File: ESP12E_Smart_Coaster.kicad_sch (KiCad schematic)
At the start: 13 parts

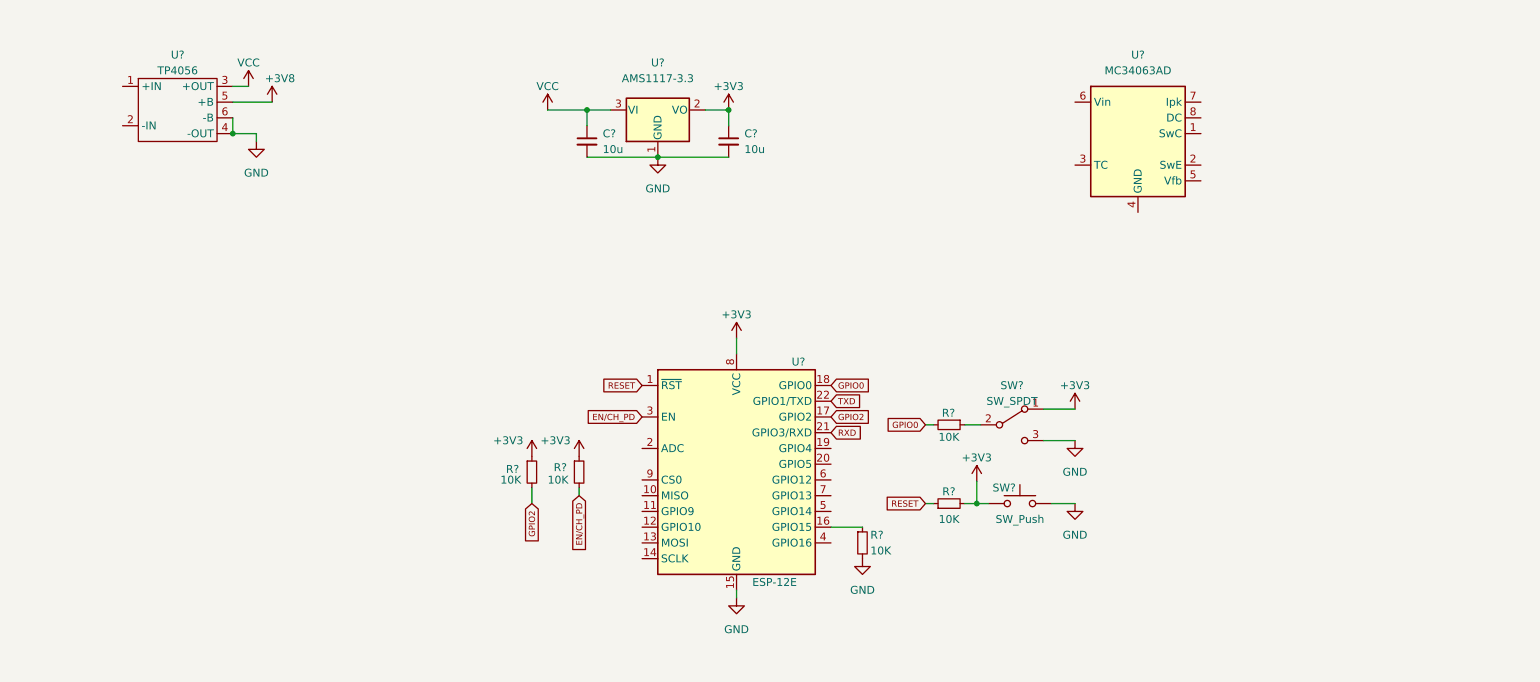
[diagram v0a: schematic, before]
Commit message: add voltage booster
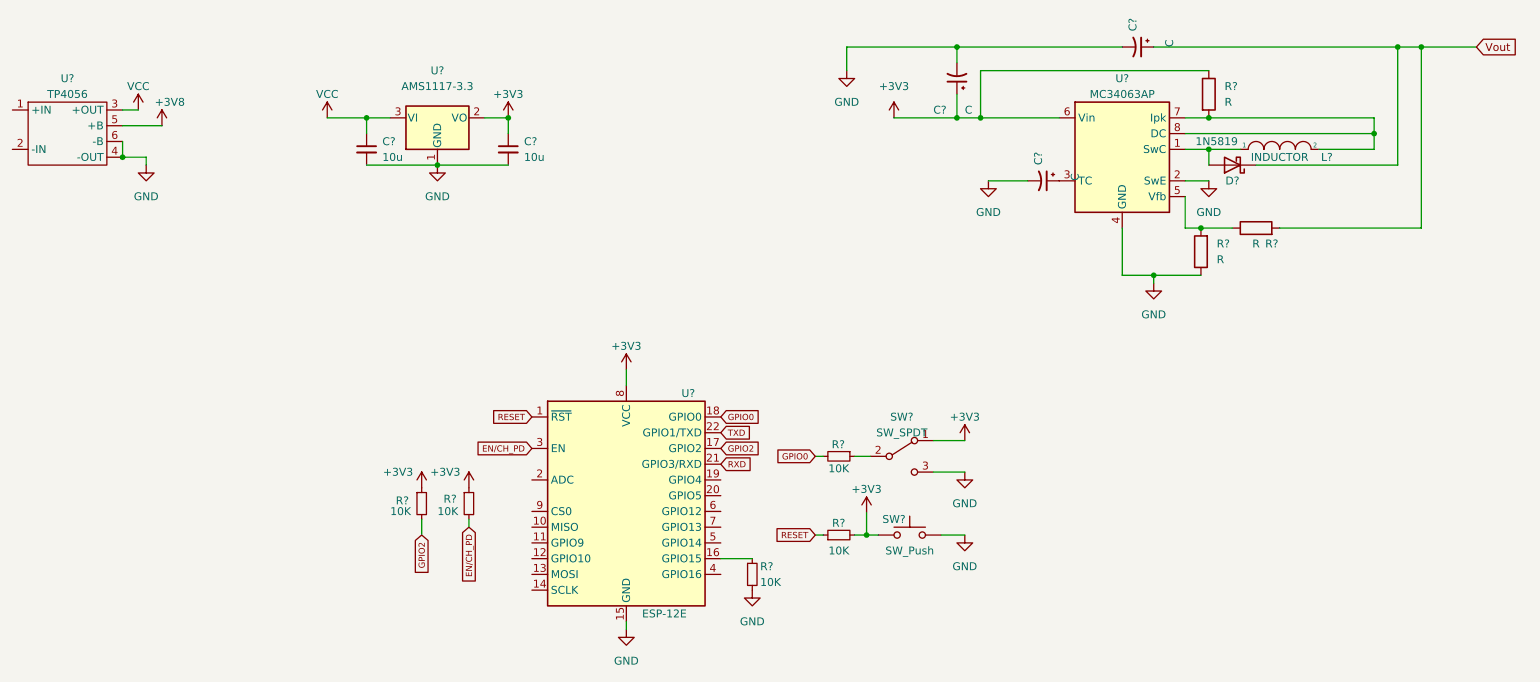
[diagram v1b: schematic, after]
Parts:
- removed U?: MC34063AD, Package_SO:SOIC-8_3.9x4.9mm_P1.27mm, symbol Regulator_Switching:MC34063AD
- added C? (x3): C, symbol Device:C_Polarized_Small_US
- added D?: 1N5819, Diode_THT:D_DO-41_SOD81_P10.16mm_Horizontal, symbol Diode:1N5819
- added L?: INDUCTOR, symbol pspice:INDUCTOR
- added R? (x3): R, symbol Device:R
- added U?: MC34063AP, Package_DIP:DIP-8_W7.62mm, symbol Regulator_Switching:MC34063AP
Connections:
- net +3V3: now also C?.1, R?.1, U?.6 (Vin)
- net GND: now also C?.2, C?.2, C?.2, R?.1, U?.2 (SwE), U?.4 (GND)
- new net: L?.2, R?.2, U?.7 (Ipk), U?.8 (DC)
- new net: D?.2 (A), L?.1, U?.1 (SwC)
- new net: C?.1, U?.3 (TC)
- new net: R?.1, R?.2, U?.5 (Vfb)
- new net Vout: C?.1, D?.1 (K), R?.2
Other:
- moved on the sheet: C?, R?, SW?, U?

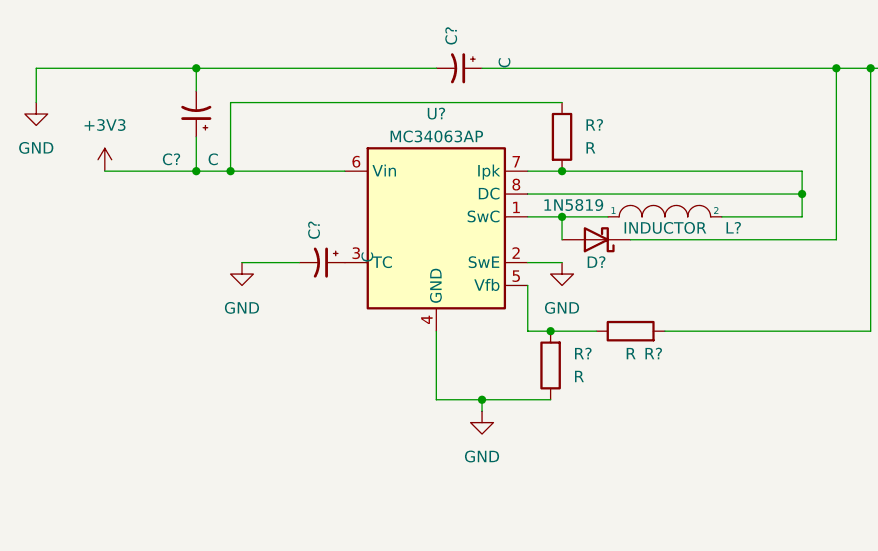
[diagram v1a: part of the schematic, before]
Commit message: add components value
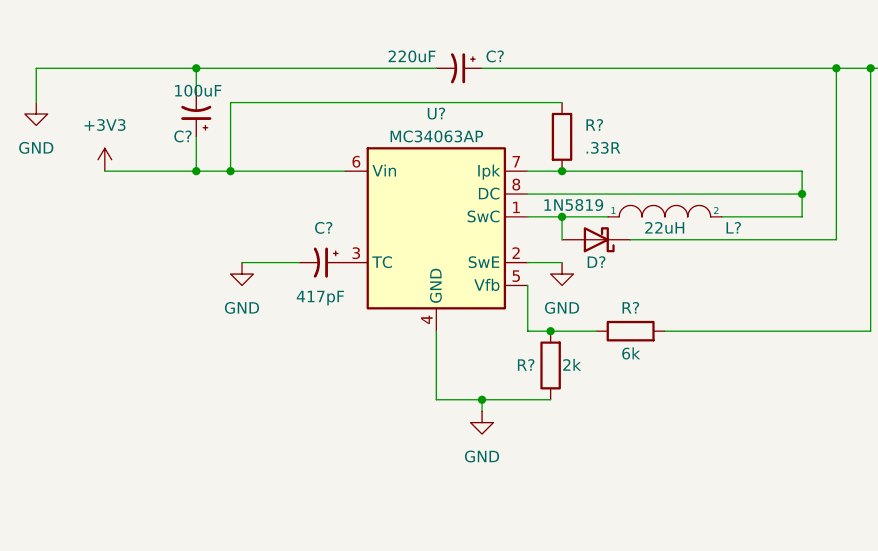
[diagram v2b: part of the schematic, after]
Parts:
- C?: value C -> 220uF
- C?: value C -> 417pF
- C?: value C -> 100uF
- L?: value INDUCTOR -> 22uH
- R?: value R -> .33R
- R?: value R -> 2k
- R?: value R -> 6k
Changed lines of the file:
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@@
   (symbol (lib_id "Device:C_Polarized_Small_US") (at 209.55 22.86 270) (unit 1)
     (in_bom yes) (on_board yes)
-    (property "Reference" "C?" (id 0) (at 208.7117 20.32 0)
+    (property "Reference" "C?" (id 0) (at 214.63 21.59 90)
       (effects (font (size 1.27 1.27)) (justify right))
     )
-    (property "Value" "C" (id 1) (at 214.63 22.86 0)
+    (property "Value" "220uF" (id 1) (at 207.01 21.59 90)
       (effects (font (size 1.27 1.27)) (justify right))
     )
@@
       (effects (font (size 1.27 1.27)) (justify left))
     )
-    (property "Value" "R" (id 1) (at 223.52 31.7499 0)
+    (property "Value" ".33R" (id 1) (at 223.52 31.7499 0)
       (effects (font (size 1.27 1.27)) (justify left))
     )
@@
   (symbol (lib_id "Device:C_Polarized_Small_US") (at 194.31 44.45 270) (unit 1)
     (in_bom yes) (on_board yes)
-    (property "Reference" "C?" (id 0) (at 193.4717 41.91 0)
+    (property "Reference" "C?" (id 0) (at 195.58 40.64 90)
       (effects (font (size 1.27 1.27)) (justify right))
     )
-    (property "Value" "C" (id 1) (at 199.39 44.45 0)
+    (property "Value" "417pF" (id 1) (at 196.85 48.26 90)
       (effects (font (size 1.27 1.27)) (justify right))
     )
@@
   )
   (symbol (lib_id "Device:R") (at 219.71 55.88 180) (unit 1)
-    (in_bom yes) (on_board yes) (fields_autoplaced)
-    (property "Reference" "R?" (id 0) (at 222.25 54.6099 0)
+    (in_bom yes) (on_board yes)
+    (property "Reference" "R?" (id 0) (at 215.9 55.88 0)
       (effects (font (size 1.27 1.27)) (justify right))
     )
-    (property "Value" "R" (id 1) (at 222.25 57.1499 0)
+    (property "Value" "2k" (id 1) (at 220.98 55.88 0)
       (effects (font (size 1.27 1.27)) (justify right))
     )
@@
   (symbol (lib_id "Device:R") (at 228.6 52.07 90) (unit 1)
     (in_bom yes) (on_board yes)
-    (property "Reference" "R?" (id 0) (at 231.14 54.61 90))
-    (property "Value" "R" (id 1) (at 228.6 54.61 90))
+    (property "Reference" "R?" (id 0) (at 228.6 49.53 90))
+    (property "Value" "6k" (id 1) (at 228.6 54.61 90))
     (property "Footprint" "" (id 2) (at 228.6 53.848 90)
       (effects (font (size 1.27 1.27)) hide)
@@
     (in_bom yes) (on_board yes)
     (property "Reference" "L?" (id 0) (at 240.03 40.64 0))
-    (property "Value" "INDUCTOR" (id 1) (at 232.41 40.64 0))
+    (property "Value" "22uH" (id 1) (at 232.41 40.64 0))
     (property "Footprint" "" (id 2) (at 232.41 39.37 0)
       (effects (font (size 1.27 1.27)) hide)
@@
   (symbol (lib_id "Device:C_Polarized_Small_US") (at 180.34 27.94 180) (unit 1)
     (in_bom yes) (on_board yes)
-    (property "Reference" "C?" (id 0) (at 176.53 33.02 0)
+    (property "Reference" "C?" (id 0) (at 177.8 30.48 0)
       (effects (font (size 1.27 1.27)) (justify right))
     )
-    (property "Value" "C" (id 1) (at 181.61 33.02 0)
+    (property "Value" "100uF" (id 1) (at 177.8 25.4 0)
       (effects (font (size 1.27 1.27)) (justify right))
     )
@@
     )
     (path "/03ffd44a-5907-4c69-ac63-01d05e10d185"
-      (reference "C?") (unit 1) (value "C") (footprint "")
+      (reference "C?") (unit 1) (value "220uF") (footprint "")
     )
     (path "/29977eb4-9adf-45f9-b113-8a6b672d0704"
@@
     )
     (path "/9a08c8ca-4c0a-4e75-ad14-947e63ea15d1"
-      (reference "C?") (unit 1) (value "C") (footprint "")
+      (reference "C?") (unit 1) (value "417pF") (footprint "")
     )
     (path "/ec0d531d-d013-4299-bad6-1fe86c606b21"
-      (reference "C?") (unit 1) (value "C") (footprint "")
+      (reference "C?") (unit 1) (value "100uF") (footprint "")
     )
     (path "/2ac1246d-9c49-4a5b-b077-d0142a22f5d7"
@@
     )
     (path "/e59b00a5-38a1-4381-bbb6-aa74cdba2304"
-      (reference "L?") (unit 1) (value "INDUCTOR") (footprint "")
+      (reference "L?") (unit 1) (value "22uH") (footprint "")
     )
     (path "/1b0e959e-9bed-4bef-ad44-07b27cb59bfc"
@@
     )
     (path "/1c0d1c3e-a71c-43a5-a634-2d8857ddc607"
-      (reference "R?") (unit 1) (value "R") (footprint "")
+      (reference "R?") (unit 1) (value ".33R") (footprint "")
     )
     (path "/28df4517-a8ac-43e7-b247-120822e55e22"
@@
     )
     (path "/a36cbb74-e982-4a7d-930e-5ed546b8c6af"
-      (reference "R?") (unit 1) (value "R") (footprint "")
+      (reference "R?") (unit 1) (value "2k") (footprint "")
     )
     (path "/bead08e4-7ff9-4dc7-b9eb-60c2c43e0b60"
-      (reference "R?") (unit 1) (value "R") (footprint "")
+      (reference "R?") (unit 1) (value "6k") (footprint "")
     )
     (path "/c13bdc96-b176-4dda-bb93-11c343b31885"
